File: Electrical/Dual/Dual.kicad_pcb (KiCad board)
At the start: 2 copper layers, 140 x 70 mm, 188 parts, among them J101 01x04, J102 02x04, J103 01x04, J104 01x03, J105 01x03, J106 01x03, J107 01x03, J108 01x03, J109 01x03, J110 01x04, J111 01x04, J112 01x04, J113 01x04, J114 01x03, J115 01x03, J116 01x03, J117 01x03, J118 02x05, J201 01x02, J202 01x04, J203 01x03, J204 01x04, J205 01x03, J206 USB_OTG, J207 01x04, J208 01x02, J209 01x04, J210 01x02, J211 01x02, J212 4PostTerm, J213 2PostTerm, J214 2PostTerm, J215 2PostTerm, J216 2PostTerm, J217 2PostTerm, J218 01x02, J219 01x02, Q201 FDC6420C, Q202 FDG1024NZ, Q301 FDC6420C, Q401 FDC6420C, U201 TPD4S012, U202 ACS712ELCTR-05B-T, U203 ACS712ELCTR-05B-T, U204 24LC256, U205 LM2576HVS-ADJ, U206 LM2576HVS-ADJ, x101 RoutaCell, x102 RoutaCell, x103 RoutaCell, x104 RoutaCell, x105 RoutaCell, x106 RoutaCell, x107 RoutaCell, x108 RoutaCell, x109 RoutaCell, x110 RoutaCell, x111 RoutaCell, x112 RoutaCell, x113 RoutaCell, x114 RoutaCell, x115 RoutaCell, x116 RoutaCell, x117 RoutaCell, x118 RoutaCell, x119 RoutaCell, x120 RoutaCell, x121 RoutaCell, x122 RoutaCell, x123 RoutaCell, x124 RoutaCell, x125 RoutaCell, x126 RoutaCell, x127 RoutaCell, x128 RoutaCell, x129 RoutaCell, x130 RoutaCell, x131 RoutaCell, x132 RoutaCell, x133 RoutaCell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

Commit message: Added ground connection to power button/reset header.
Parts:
- J201: value 01x02 -> 01x03; footprint Pin_Headers:Pin_Header_Straight_1x02_Pitch2.54mm -> Pin_Headers:Pin_Header_Straight_1x03_Pitch2.54mm
- renumbered J118 to x100
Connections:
- A201 pad 1.17: Net-(A201-Pad1.17) -> (no net)
- A201 pad 1.18: Net-(A201-Pad1.18) -> (no net)
- A201 pad 2.14: Net-(A201-Pad2.14) -> (no net)
- A201 pad 2.16: Net-(A201-Pad2.16) -> (no net)
- J201 pad 2: Net-(A201-Pad2.26) -> GND
- RN201 pad 6: Net-(RN201-Pad6) -> (no net)
- U201 pad 5: Net-(U201-Pad5) -> (no net)
- x100 pad 1: Net-(J118-Pad1) -> (no net)
- x100 pad 10: Net-(J118-Pad10) -> (no net)
- x100 pad 2: Net-(J118-Pad2) -> (no net)
- x100 pad 3: Net-(J118-Pad3) -> (no net)
- x100 pad 4: Net-(J118-Pad4) -> (no net)
- x100 pad 5: Net-(J118-Pad5) -> (no net)
- x100 pad 6: Net-(J118-Pad6) -> (no net)
- x100 pad 7: Net-(J118-Pad7) -> (no net)
- x100 pad 8: Net-(J118-Pad8) -> (no net)
- x100 pad 9: Net-(J118-Pad9) -> (no net)
- x101 pad D: Net-(J118-Pad2) -> Net-(x100-Pad2)
- x101 pad U: Net-(J118-Pad1) -> Net-(x100-Pad1)
- x102 pad D: Net-(J118-Pad2) -> Net-(x100-Pad2)
- x102 pad U: Net-(J118-Pad1) -> Net-(x100-Pad1)
- x103 pad D: Net-(J118-Pad2) -> Net-(x100-Pad2)
- x103 pad U: Net-(J118-Pad1) -> Net-(x100-Pad1)
- x104 pad D: Net-(J118-Pad2) -> Net-(x100-Pad2)
- x104 pad U: Net-(J118-Pad1) -> Net-(x100-Pad1)
- x105 pad D: Net-(J118-Pad2) -> Net-(x100-Pad2)
- x105 pad U: Net-(J118-Pad1) -> Net-(x100-Pad1)
- x106 pad D: Net-(J118-Pad2) -> Net-(x100-Pad2)
- x106 pad U: Net-(J118-Pad1) -> Net-(x100-Pad1)
- x107 pad D: Net-(J118-Pad2) -> Net-(x100-Pad2)
- x107 pad U: Net-(J118-Pad1) -> Net-(x100-Pad1)
- x108 pad D: Net-(J118-Pad2) -> Net-(x100-Pad2)
- x108 pad U: Net-(J118-Pad1) -> Net-(x100-Pad1)
- x109 pad D: Net-(J118-Pad2) -> Net-(x100-Pad2)
- x109 pad U: Net-(J118-Pad1) -> Net-(x100-Pad1)
- x110 pad D: Net-(J118-Pad2) -> Net-(x100-Pad2)
- x110 pad U: Net-(J118-Pad1) -> Net-(x100-Pad1)
- x111 pad D: Net-(J118-Pad2) -> Net-(x100-Pad2)
- x111 pad U: Net-(J118-Pad1) -> Net-(x100-Pad1)
- x112 pad D: Net-(J118-Pad2) -> Net-(x100-Pad2)
- x112 pad U: Net-(J118-Pad1) -> Net-(x100-Pad1)
- x113 pad D: Net-(J118-Pad4) -> Net-(x100-Pad4)
- x113 pad U: Net-(J118-Pad3) -> Net-(x100-Pad3)
- x114 pad D: Net-(J118-Pad4) -> Net-(x100-Pad4)
- x114 pad U: Net-(J118-Pad3) -> Net-(x100-Pad3)
- x115 pad D: Net-(J118-Pad4) -> Net-(x100-Pad4)
- x115 pad U: Net-(J118-Pad3) -> Net-(x100-Pad3)
- x116 pad D: Net-(J118-Pad4) -> Net-(x100-Pad4)
- x116 pad U: Net-(J118-Pad3) -> Net-(x100-Pad3)
- x117 pad D: Net-(J118-Pad4) -> Net-(x100-Pad4)
- x117 pad U: Net-(J118-Pad3) -> Net-(x100-Pad3)
- x118 pad D: Net-(J118-Pad4) -> Net-(x100-Pad4)
- x118 pad U: Net-(J118-Pad3) -> Net-(x100-Pad3)
- x119 pad D: Net-(J118-Pad4) -> Net-(x100-Pad4)
- x119 pad U: Net-(J118-Pad3) -> Net-(x100-Pad3)
- x120 pad D: Net-(J118-Pad4) -> Net-(x100-Pad4)
- x120 pad U: Net-(J118-Pad3) -> Net-(x100-Pad3)
- x121 pad D: Net-(J118-Pad4) -> Net-(x100-Pad4)
- x121 pad U: Net-(J118-Pad3) -> Net-(x100-Pad3)
- x122 pad D: Net-(J118-Pad4) -> Net-(x100-Pad4)
- x122 pad U: Net-(J118-Pad3) -> Net-(x100-Pad3)
- x123 pad D: Net-(J118-Pad4) -> Net-(x100-Pad4)
- x123 pad U: Net-(J118-Pad3) -> Net-(x100-Pad3)
- x124 pad D: Net-(J118-Pad4) -> Net-(x100-Pad4)
- x124 pad U: Net-(J118-Pad3) -> Net-(x100-Pad3)
- x125 pad D: Net-(J118-Pad6) -> Net-(x100-Pad6)
- x125 pad U: Net-(J118-Pad5) -> Net-(x100-Pad5)
- x126 pad D: Net-(J118-Pad6) -> Net-(x100-Pad6)
- x126 pad U: Net-(J118-Pad5) -> Net-(x100-Pad5)
- x127 pad D: Net-(J118-Pad6) -> Net-(x100-Pad6)
- x127 pad U: Net-(J118-Pad5) -> Net-(x100-Pad5)
- x128 pad D: Net-(J118-Pad6) -> Net-(x100-Pad6)
- x128 pad U: Net-(J118-Pad5) -> Net-(x100-Pad5)
- x129 pad D: Net-(J118-Pad6) -> Net-(x100-Pad6)
- x129 pad U: Net-(J118-Pad5) -> Net-(x100-Pad5)
- x130 pad D: Net-(J118-Pad6) -> Net-(x100-Pad6)
- x130 pad U: Net-(J118-Pad5) -> Net-(x100-Pad5)
- x131 pad D: Net-(J118-Pad6) -> Net-(x100-Pad6)
- x131 pad U: Net-(J118-Pad5) -> Net-(x100-Pad5)
- x132 pad D: Net-(J118-Pad6) -> Net-(x100-Pad6)
- x132 pad U: Net-(J118-Pad5) -> Net-(x100-Pad5)
- x133 pad D: Net-(J118-Pad6) -> Net-(x100-Pad6)
- x133 pad U: Net-(J118-Pad5) -> Net-(x100-Pad5)
- x134 pad D: Net-(J118-Pad6) -> Net-(x100-Pad6)
- x134 pad U: Net-(J118-Pad5) -> Net-(x100-Pad5)
- x135 pad D: Net-(J118-Pad6) -> Net-(x100-Pad6)
- x135 pad U: Net-(J118-Pad5) -> Net-(x100-Pad5)
- x136 pad D: Net-(J118-Pad6) -> Net-(x100-Pad6)
- x136 pad U: Net-(J118-Pad5) -> Net-(x100-Pad5)
- x137 pad D: Net-(J118-Pad8) -> Net-(x100-Pad8)
- x137 pad U: Net-(J118-Pad7) -> Net-(x100-Pad7)
- x138 pad D: Net-(J118-Pad8) -> Net-(x100-Pad8)
- x138 pad U: Net-(J118-Pad7) -> Net-(x100-Pad7)
- x139 pad D: Net-(J118-Pad8) -> Net-(x100-Pad8)
- x139 pad U: Net-(J118-Pad7) -> Net-(x100-Pad7)
- x140 pad D: Net-(J118-Pad8) -> Net-(x100-Pad8)
- x140 pad U: Net-(J118-Pad7) -> Net-(x100-Pad7)
- x141 pad D: Net-(J118-Pad8) -> Net-(x100-Pad8)
- x141 pad U: Net-(J118-Pad7) -> Net-(x100-Pad7)
- x142 pad D: Net-(J118-Pad8) -> Net-(x100-Pad8)
- x142 pad U: Net-(J118-Pad7) -> Net-(x100-Pad7)
- x143 pad D: Net-(J118-Pad8) -> Net-(x100-Pad8)
- x143 pad U: Net-(J118-Pad7) -> Net-(x100-Pad7)
- x144 pad D: Net-(J118-Pad8) -> Net-(x100-Pad8)
- x144 pad U: Net-(J118-Pad7) -> Net-(x100-Pad7)
- x145 pad D: Net-(J118-Pad8) -> Net-(x100-Pad8)
- x145 pad U: Net-(J118-Pad7) -> Net-(x100-Pad7)
- x146 pad D: Net-(J118-Pad8) -> Net-(x100-Pad8)
- x146 pad U: Net-(J118-Pad7) -> Net-(x100-Pad7)
- x147 pad D: Net-(J118-Pad8) -> Net-(x100-Pad8)
- x147 pad U: Net-(J118-Pad7) -> Net-(x100-Pad7)
- x148 pad D: Net-(J118-Pad8) -> Net-(x100-Pad8)
- x148 pad U: Net-(J118-Pad7) -> Net-(x100-Pad7)
- x149 pad D: Net-(J118-Pad10) -> Net-(x100-Pad10)
- x149 pad U: Net-(J118-Pad9) -> Net-(x100-Pad9)
- x150 pad D: Net-(J118-Pad10) -> Net-(x100-Pad10)
- x150 pad U: Net-(J118-Pad9) -> Net-(x100-Pad9)
- x151 pad D: Net-(J118-Pad10) -> Net-(x100-Pad10)
- x151 pad U: Net-(J118-Pad9) -> Net-(x100-Pad9)
- x152 pad D: Net-(J118-Pad10) -> Net-(x100-Pad10)
- x152 pad U: Net-(J118-Pad9) -> Net-(x100-Pad9)
- x153 pad D: Net-(J118-Pad10) -> Net-(x100-Pad10)
- x153 pad U: Net-(J118-Pad9) -> Net-(x100-Pad9)
- x154 pad D: Net-(J118-Pad10) -> Net-(x100-Pad10)
- x154 pad U: Net-(J118-Pad9) -> Net-(x100-Pad9)
- x155 pad D: Net-(J118-Pad10) -> Net-(x100-Pad10)
- x155 pad U: Net-(J118-Pad9) -> Net-(x100-Pad9)
- x156 pad D: Net-(J118-Pad10) -> Net-(x100-Pad10)
- x156 pad U: Net-(J118-Pad9) -> Net-(x100-Pad9)
- x157 pad D: Net-(J118-Pad10) -> Net-(x100-Pad10)
- x157 pad U: Net-(J118-Pad9) -> Net-(x100-Pad9)
- x158 pad D: Net-(J118-Pad10) -> Net-(x100-Pad10)
- x158 pad U: Net-(J118-Pad9) -> Net-(x100-Pad9)
- x159 pad D: Net-(J118-Pad10) -> Net-(x100-Pad10)
- x159 pad U: Net-(J118-Pad9) -> Net-(x100-Pad9)
- x160 pad D: Net-(J118-Pad10) -> Net-(x100-Pad10)
- x160 pad U: Net-(J118-Pad9) -> Net-(x100-Pad9)
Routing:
- net Net-(J118-Pad8): track 73.1 -> 0.00 mm
- net Net-(x100-Pad8): track 0.00 -> 72.3 mm
- net Net-(x100-Pad2): track 0.00 -> 69.6 mm
- net Net-(J118-Pad2): track 69.6 -> 0.00 mm
- net Net-(x100-Pad1): track 0.00 -> 69.2 mm
- net Net-(J118-Pad1): track 69.2 -> 0.00 mm
- net Net-(x100-Pad5): track 0.00 -> 68.9 mm
- net Net-(J118-Pad5): track 68.9 -> 0.00 mm
- net Net-(x100-Pad7): track 0.00 -> 68.1 mm
- net Net-(J118-Pad7): track 68.1 -> 0.00 mm
- net Net-(x100-Pad3): track 0.00 -> 66.8 mm
- net Net-(J118-Pad3): track 66.8 -> 0.00 mm
- net Net-(x100-Pad4): track 0.00 -> 66.6 mm
- net Net-(J118-Pad4): track 66.6 -> 0.00 mm
- net Net-(x100-Pad6): track 0.00 -> 64.3 mm
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
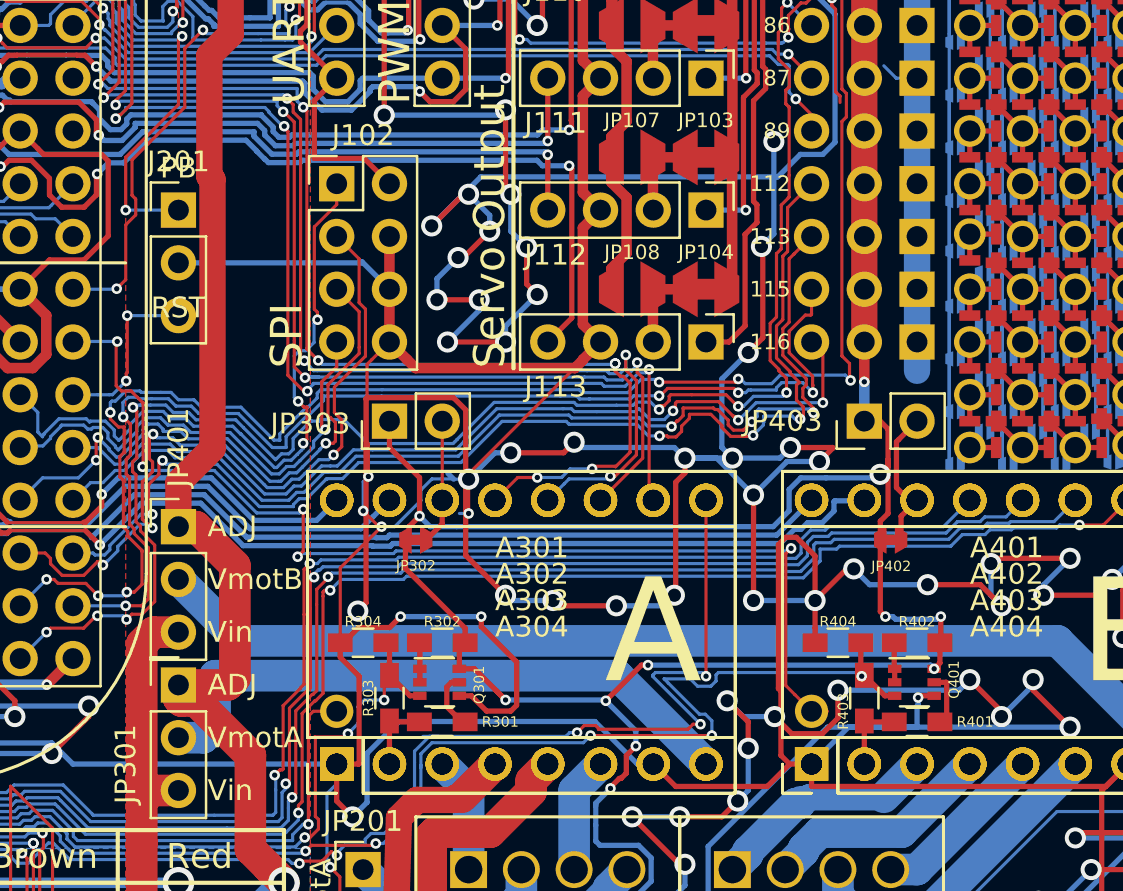
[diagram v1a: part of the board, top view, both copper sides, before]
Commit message: Added a diode to the stepper fault/3v3 supply to ensure fault remains low when RESET/PMIC_OUT_PGOOD is low.
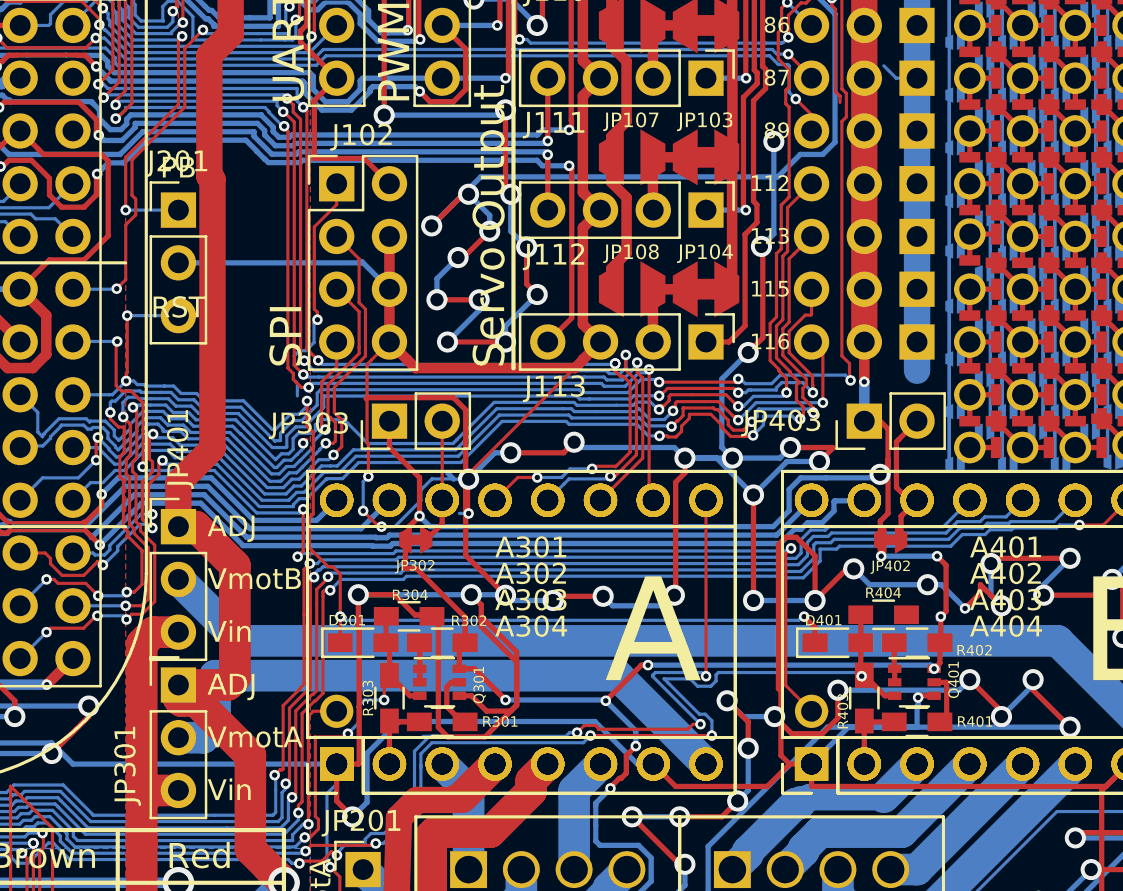
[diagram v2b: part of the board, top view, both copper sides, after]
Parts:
- added D301: D, footprints:D_0603_HandSoldering, F.Cu at (127.9, 113.2)
- added D401: D, footprints:D_0603_HandSoldering, F.Cu at (150.8, 113.2)
- moved R404 2.58 mm to (153.0, 111.9), turned to 0 degrees
- moved R304 2.56 mm to (130.2, 111.9), turned to 0 degrees
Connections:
- net Net-(A201-Pad2.26) renamed RST
- x100 pad 1: (no net) -> Net-(x100-Pad1)
- x100 pad 10: (no net) -> Net-(x100-Pad10)
- x100 pad 2: (no net) -> Net-(x100-Pad2)
- x100 pad 3: (no net) -> Net-(x100-Pad3)
- x100 pad 4: (no net) -> Net-(x100-Pad4)
- x100 pad 5: (no net) -> Net-(x100-Pad5)
- x100 pad 6: (no net) -> Net-(x100-Pad6)
- x100 pad 7: (no net) -> Net-(x100-Pad7)
- x100 pad 8: (no net) -> Net-(x100-Pad8)
- x100 pad 9: (no net) -> Net-(x100-Pad9)
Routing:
- net RST: track 8.47 -> 55.5 mm, vias 2 -> 5
- net GND: track 2753.7 -> 2758.4 mm
- net /spi1_d1: track 32.6 -> 28.7 mm, vias 3 -> 2
- net /Common/gpio0_4: track 125.2 -> 126.6 mm
- net /Common/gpio0_5: track 106.3 -> 107.6 mm
- net Net-(x100-Pad8): track 72.3 -> 73.1 mm
- net 3V3S: track 338.2 -> 338.8 mm, vias 30 -> 31

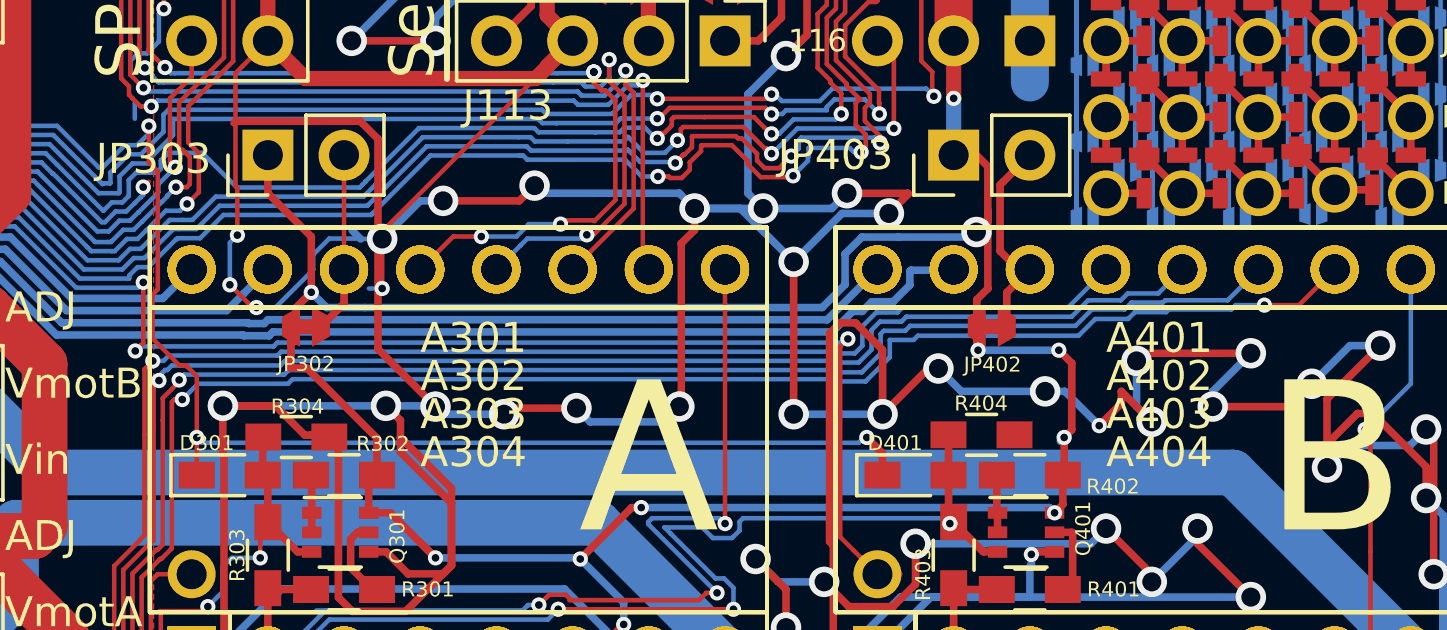
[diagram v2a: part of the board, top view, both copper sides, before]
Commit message: Switched two pins for easier routing on quad board.
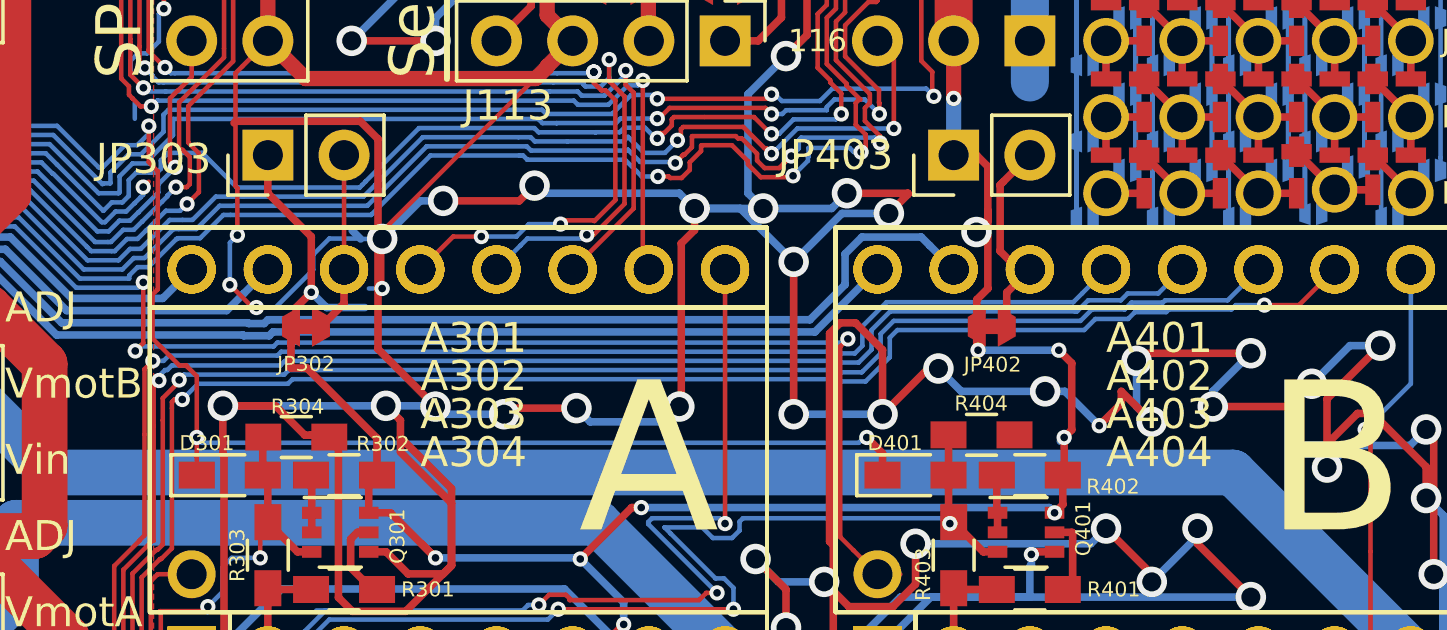
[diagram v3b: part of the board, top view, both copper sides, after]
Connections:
- A401 pad 15: /Common/pr1_pru1_pru_r30_15 -> /Common/pr1_pru1_pru_r30_14
- A401 pad 16: /Common/pr1_pru1_pru_r30_14 -> /Common/pr1_pru1_pru_r30_15
- A402 pad 15: /Common/pr1_pru1_pru_r30_15 -> /Common/pr1_pru1_pru_r30_14
- A402 pad 16: /Common/pr1_pru1_pru_r30_14 -> /Common/pr1_pru1_pru_r30_15
- A403 pad 15: /Common/pr1_pru1_pru_r30_15 -> /Common/pr1_pru1_pru_r30_14
- A403 pad 16: /Common/pr1_pru1_pru_r30_14 -> /Common/pr1_pru1_pru_r30_15
- A404 pad 15: /Common/pr1_pru1_pru_r30_15 -> /Common/pr1_pru1_pru_r30_14
- A404 pad 16: /Common/pr1_pru1_pru_r30_14 -> /Common/pr1_pru1_pru_r30_15
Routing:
- net 3V3S: track 338.8 -> 316.8 mm
- net /Common/pr1_pru1_pru_r30_14: track 64.0 -> 68.0 mm
- net /Common/pr1_pru1_pru_r30_15: track 68.0 -> 64.7 mm

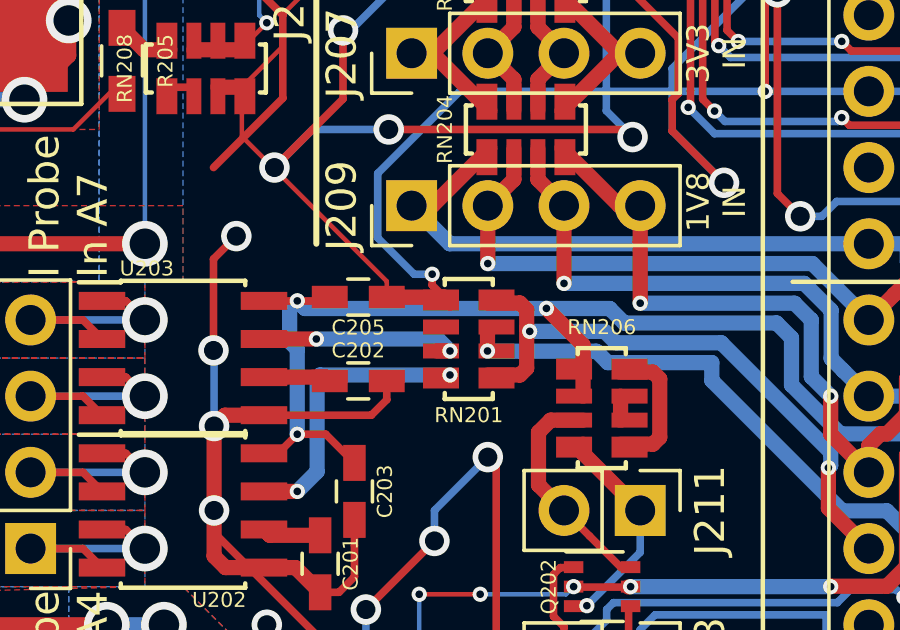
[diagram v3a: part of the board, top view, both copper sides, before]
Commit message: fixed unconnected pad 6 on RN201
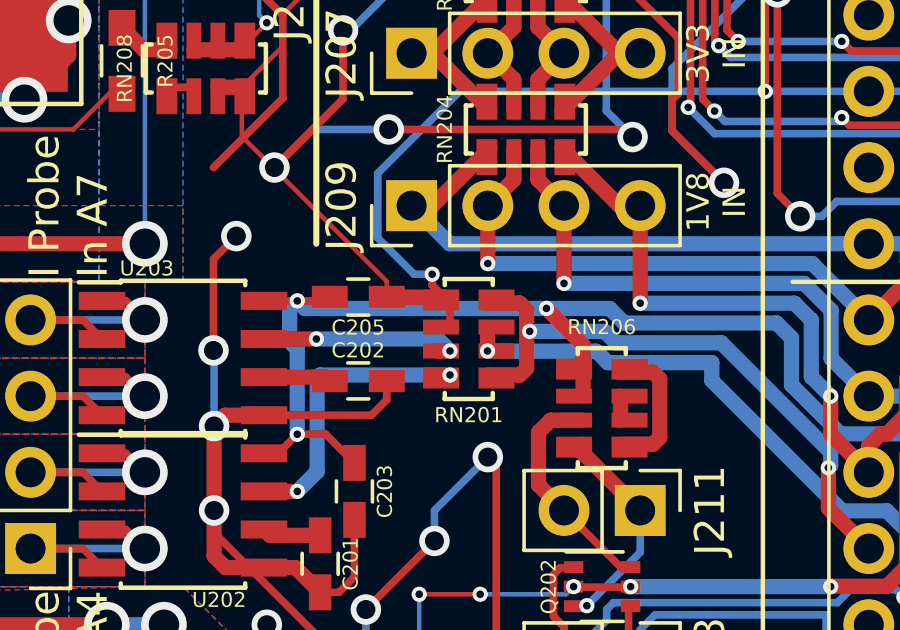
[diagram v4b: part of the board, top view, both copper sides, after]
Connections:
- RN201 pad 6: (no net) -> GND
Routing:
- net GND: track 2758.4 -> 2759.2 mm
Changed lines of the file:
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@@
 (kicad_pcb (version 4) (host pcbnew 4.0.7)
   (general
-    (links 627)
-    (no_connects 3)
+    (links 628)
+    (no_connects 2)
     (area 29.695199 64.695199 170.304801 135.304801)
     (thickness 1.6)
     (drawings 284)
-    (tracks 5727)
+    (tracks 5728)
     (zones 0)
     (modules 190)
@@
     (pad 3 smd rect (at 0.4 0.625 90) (size 0.5 1.2) (drill (offset 0 0.3)) (layers F.Cu F.Paste F.Mask)
       (net 109 /Common/ain7))
-    (pad 6 smd rect (at 0.4 -0.625 270) (size 0.5 1.2) (drill (offset 0 0.3)) (layers F.Cu F.Paste F.Mask))
+    (pad 6 smd rect (at 0.4 -0.625 270) (size 0.5 1.2) (drill (offset 0 0.3)) (layers F.Cu F.Paste F.Mask)
+      (net 1 GND))
     (pad 7 smd rect (at -0.4 -0.625 270) (size 0.5 1.2) (drill (offset 0 0.3)) (layers F.Cu F.Paste F.Mask)
       (net 124 "Net-(RN201-Pad7)"))
@@
   (via (at 49.2 98.73) (size 1.016) (drill 0.635) (layers F.Cu B.Cu) (net 0))
   (segment (start 124.775023 101.32827) (end 124.775023 100.789838) (width 0.1524) (layer B.Cu) (net 0))
+  (segment (start 72.07 95.625) (end 72.07 96.425) (width 0.254) (layer F.Cu) (net 1))
   (segment (start 139.497 110.9728) (end 137.2872 110.9728) (width 0.254) (layer F.Cu) (net 1))
   (segment (start 137.2872 110.9728) (end 137.084 111.176) (width 0.254) (layer F.Cu) (net 1))
